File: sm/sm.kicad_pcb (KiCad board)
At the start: 2 copper layers, 102 x 137 mm, 165 parts, among them M1 TPS61040, M2 LM5164, M3 STM32F405RG, M4 TPS73633, M5 UCC27211A, M6 UCC27211A, M7 UCC27211A, M8 SN65HVD256, P1 USART, P2 SWD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

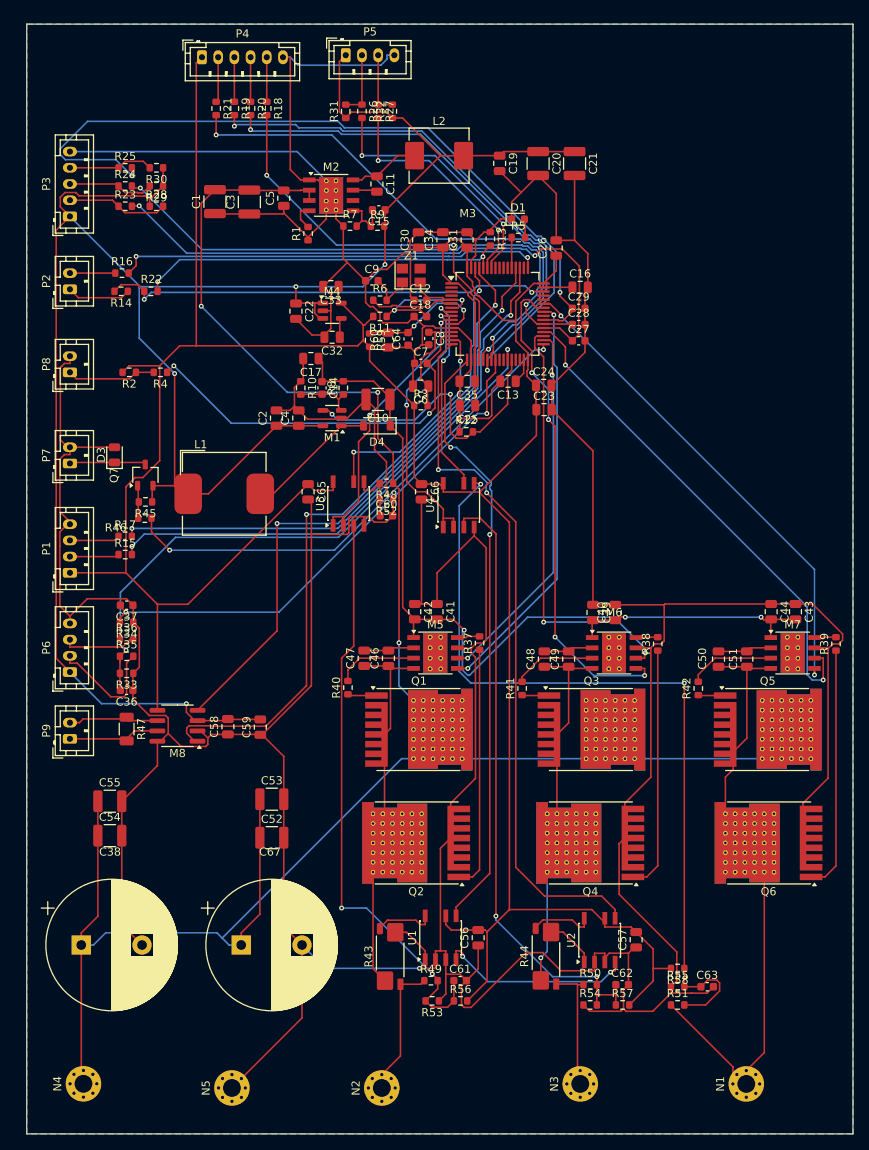
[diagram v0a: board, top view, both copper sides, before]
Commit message: Change location of the ports
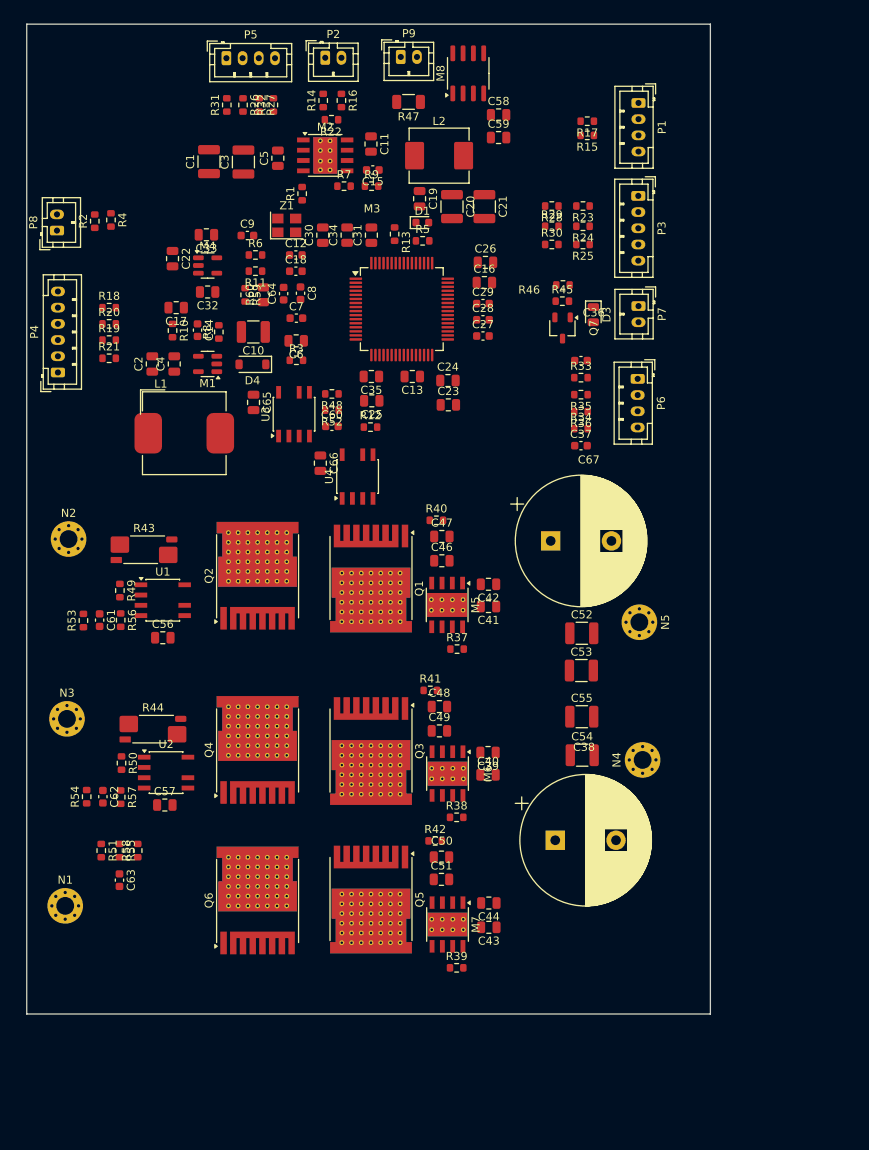
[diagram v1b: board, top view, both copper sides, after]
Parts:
- moved P9 93.6 mm to (149.2, 22.1), turned to 0 degrees
- moved P1 91.1 mm to (178.5, 27.7), turned to -90 degrees
- moved M8 88.2 mm to (157.5, 24.1), turned to 90 degrees
- moved N1 86.9 mm to (107.8, 126.8), turned to 0 degrees
- moved R47 84.9 mm to (150.1, 27.6), turned to 180 degrees
- moved C58 82.6 mm to (161.2, 29.2), turned to 0 degrees
- moved N4 79.8 mm to (179.0, 108.8)
- moved P6 78.9 mm to (178.4, 61.8), turned to -90 degrees
- moved C59 78.5 mm to (161.2, 32.0), turned to 0 degrees
- moved N2 78.0 mm to (108.2, 81.6), turned to 0 degrees
- moved N3 77.8 mm to (108.0, 103.8), turned to 0 degrees
- moved R15 77.0 mm to (172.2, 31.7), turned to 180 degrees
- moved R17 76.7 mm to (172.2, 30.0), turned to 180 degrees
- moved N5 76.4 mm to (178.6, 91.8), turned to -90 degrees
- moved C63 73.7 mm to (114.5, 123.7), turned to -90 degrees
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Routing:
- net GND: track 836.3 -> 0.00 mm, vias 1 -> 0
- net +48V: track 391.9 -> 0.00 mm, vias 3 -> 0
- net +3.3V: track 370.0 -> 0.00 mm
- net +5V: track 265.0 -> 0.00 mm, vias 4 -> 0
- net TERMINAL_C: track 127.0 -> 0.00 mm
- net +12V: track 107.9 -> 0.00 mm, vias 3 -> 0
- net Net-(U4B-+): track 101.9 -> 0.00 mm, vias 2 -> 0
- net Net-(M3-PC8/TIM3_CH3): track 93.3 -> 0.00 mm, vias 2 -> 0
- net Net-(M5-HS): track 88.1 -> 0.00 mm
- net Net-(M6-HS): track 88.0 -> 0.00 mm, vias 1 -> 0
- net CURRENT_B: track 87.4 -> 0.00 mm, vias 2 -> 0
- net CAN_TX: track 82.6 -> 0.00 mm, vias 2 -> 0
- net Net-(U4A-+): track 77.2 -> 0.00 mm, vias 2 -> 0
- net ADC_ANG: track 76.3 -> 0.00 mm, vias 2 -> 0
- net CAN_RX: track 75.1 -> 0.00 mm, vias 2 -> 0
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- removed copper zone on B.Cu, net GND
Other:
- board size 102 x 137 mm -> 84.4 x 122.2 mm

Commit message: Use freerouting
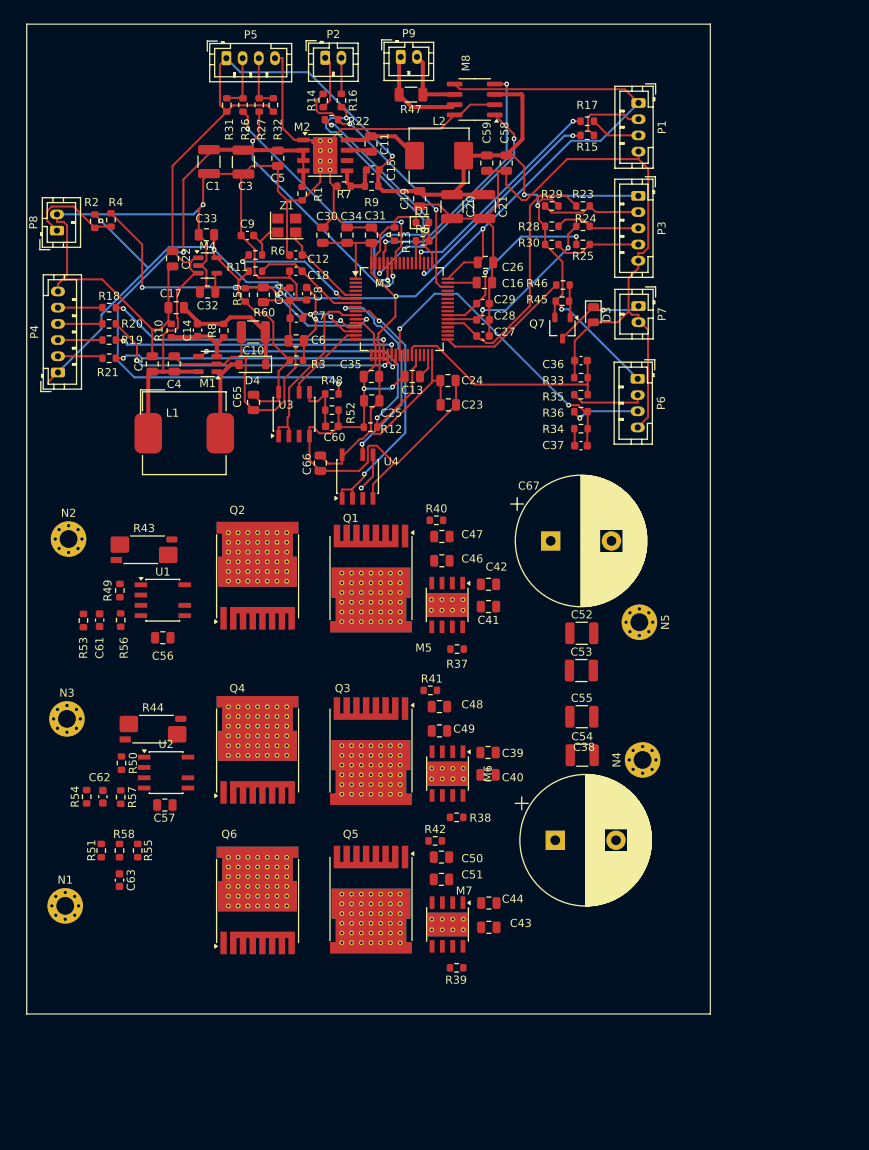
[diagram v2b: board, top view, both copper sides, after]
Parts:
- moved C58 6.03 mm to (162.2, 35.1), turned to 90 degrees
- moved C59 3.47 mm to (159.8, 35.1), turned to 90 degrees
- moved M8 3.32 mm to (158.3, 27.3), turned to 180 degrees
- moved R47 0.95 mm to (150.4, 26.7)
- moved C64 0.76 mm to (135.5, 51.3)
- moved C8 0.76 mm to (137.6, 51.3)
- moved R8 0.63 mm to (127.3, 55.8)
- moved R10 0.15 mm to (120.8, 55.8)
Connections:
- C1 pad 2: +48V -> Net-(M2-RON)
- C3 pad 2: +48V -> Net-(M2-RON)
- C5 pad 2: +48V -> Net-(M2-RON)
- M2 pad 2: +48V -> Net-(M2-RON)
- M2 pad 3: +48V -> Net-(M2-RON)
- Q1 pad 3: +48V -> Net-(M2-RON)
- R48 pad 1: +48V -> Net-(M2-RON)
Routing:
- net GND: track 0.00 -> 412.9 mm, vias 0 -> 3
- net +3.3V: track 0.00 -> 229.5 mm, vias 0 -> 4
- net +5V: track 0.00 -> 187.9 mm, vias 0 -> 4
- net Net-(M2-RON): track 0.00 -> 77.9 mm, vias 0 -> 2
- net 12V_EN: track 0.00 -> 45.2 mm, vias 0 -> 2
- net Net-(M3-PA0/WKUP/ADC_IN0): track 0.00 -> 40.6 mm, vias 0 -> 3
- net ADC_BRK: track 0.00 -> 38.5 mm, vias 0 -> 2
- net Net-(M3-PA5/SPI1_SCK/DAC_OUT2): track 0.00 -> 37.9 mm, vias 0 -> 2
- net Net-(M3-PA7/SPI1_MOSI): track 0.00 -> 36.6 mm, vias 0 -> 2
- net Net-(M3-PA4/SPI1_NSS/DAC_OUT1): track 0.00 -> 36.6 mm, vias 0 -> 2
- net BOOT: track 0.00 -> 35.6 mm, vias 0 -> 3
- net Net-(M3-PA6/SPI1_MISO): track 0.00 -> 35.6 mm, vias 0 -> 2
- net Net-(M3-PA13/SWDIO): track 0.00 -> 32.9 mm, vias 0 -> 2
- net CAN_RX: track 0.00 -> 32.7 mm, vias 0 -> 2
- net Net-(M3-PB7/I2C1_SDA/TIM4_CH2): track 0.00 -> 32.6 mm, vias 0 -> 2
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
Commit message: Trace tracks
Select components
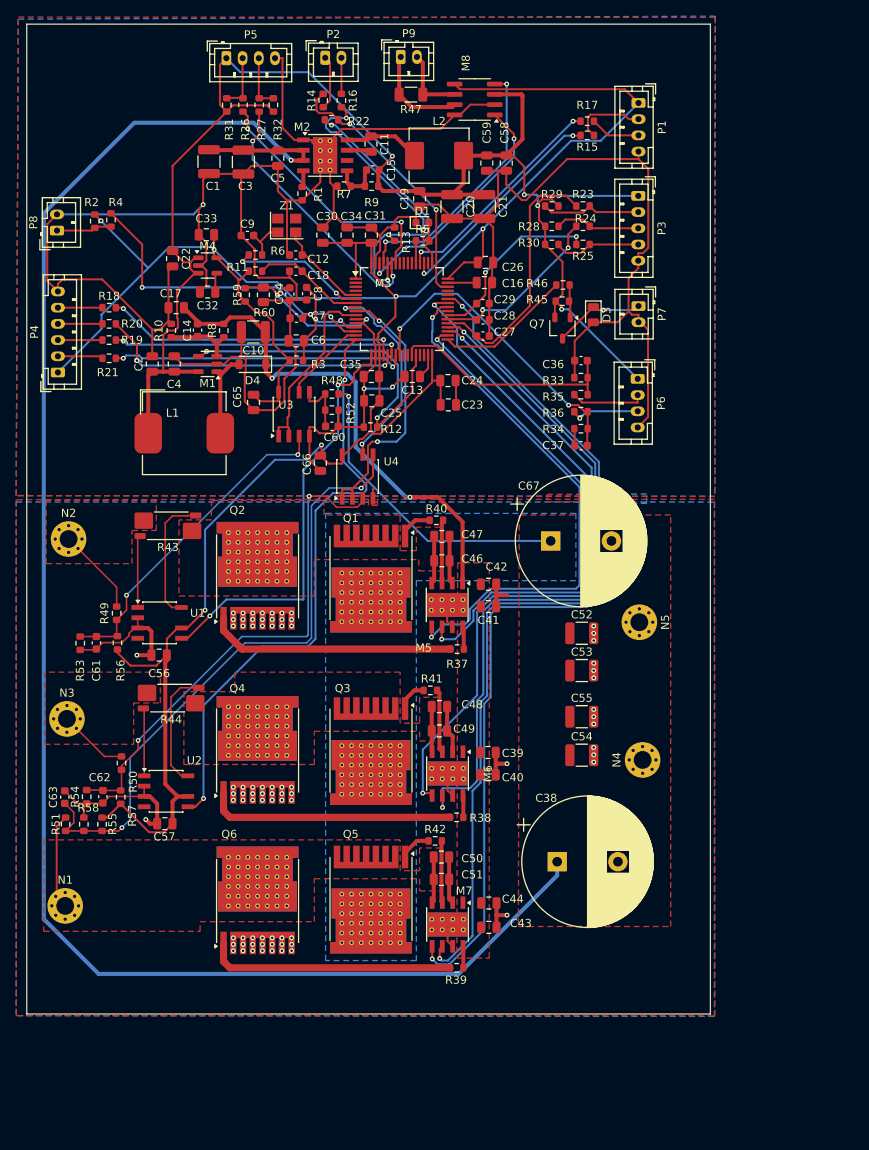
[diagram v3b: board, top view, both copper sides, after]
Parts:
- moved C63 12.3 mm to (107.7, 113.4), turned to 90 degrees
- moved R51 5.47 mm to (107.8, 116.8)
- moved R55 5.47 mm to (110.0, 116.8)
- moved R58 5.47 mm to (112.3, 116.8)
- moved R44 4.44 mm to (120.8, 101.2), turned to 180 degrees
- moved R43 4.17 mm to (120.4, 79.9), turned to 180 degrees
- moved U1 2.83 mm to (119.4, 91.9)
- moved C61 2.83 mm to (111.6, 94.4)
- moved R49 2.83 mm to (114.1, 90.7)
- moved R53 2.83 mm to (109.6, 94.4)
- moved R56 2.83 mm to (114.2, 94.4)
- moved C38 2.66 mm to (168.5, 121.4)
- moved C57 2.30 mm to (120.0, 116.7)
- moved U2 2.30 mm to (120.2, 112.7)
- moved C56 2.20 mm to (119.3, 95.9)
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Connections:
- C1 pad 2: Net-(M2-RON) -> +48V
- C3 pad 2: Net-(M2-RON) -> +48V
- C5 pad 2: Net-(M2-RON) -> +48V
- M2 pad 2: Net-(M2-RON) -> +48V
- M2 pad 3: Net-(M2-RON) -> +48V
- M5 pad 9: (no net) -> GND
- M6 pad 9: (no net) -> GND
- M7 pad 9: (no net) -> GND
- Q1 pad 3: Net-(M2-RON) -> +48V
- R43 pad 2: TERMINAL_A -> Net-(U1-+)
- R43 pad 3: Net-(U1-+) -> Net-(U1-_)
- R43 pad 4: Net-(U1-_) -> TERMINAL_A
- R44 pad 2: TERMINAL_B -> Net-(U2-+)
- R44 pad 3: Net-(U2-+) -> Net-(U2-_)
- R44 pad 4: Net-(U2-_) -> TERMINAL_B
- R48 pad 1: Net-(M2-RON) -> +48V
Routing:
- net +48V: track 0.00 -> 250.8 mm, vias 0 -> 2
- net FET_CH: track 0.01 -> 108.4 mm, vias 0 -> 2
- net FET_CL: track 0.00 -> 103.3 mm, vias 0 -> 2
- net FET_BH: track 0.00 -> 85.9 mm, vias 0 -> 2
- net FET_BL: track 0.00 -> 84.2 mm, vias 0 -> 2
- net +3.3V: track 229.5 -> 307.4 mm, vias 4 -> 6
- net Net-(M2-RON): track 77.9 -> 2.06 mm, vias 2 -> 0
- net CURRENT_B: track 0.75 -> 75.4 mm, vias 0 -> 2
- net Net-(U4B-+): track 4.72 -> 77.1 mm, vias 1 -> 2
- net FET_AH: track 0.00 -> 66.3 mm, vias 0 -> 2
- net Net-(U4A-+): track 0.00 -> 62.7 mm, vias 0 -> 2
- net FET_AL: track 0.00 -> 62.2 mm, vias 0 -> 2
- net CURRENT_A: track 0.00 -> 52.0 mm, vias 0 -> 2
- net +12V: track 16.2 -> 61.8 mm, vias 0 -> 2
- net Net-(U3A-+): track 0.00 -> 40.9 mm, vias 0 -> 2
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- added copper zone on F.Cu, net +12V
- added copper zone on B.Cu, net +48V
- added copper zone on F.Cu, net +48V
- added copper zone on B.Cu, net GND
- added copper zone on F.Cu, net GND
- added copper zone on F.Cu, net Net-(M5-HS)
- added copper zone on F.Cu, net Net-(M6-HS)
- added copper zone on F.Cu, net TERMINAL_A
- added copper zone on F.Cu, net TERMINAL_B
- added copper zone on F.Cu, net TERMINAL_C
